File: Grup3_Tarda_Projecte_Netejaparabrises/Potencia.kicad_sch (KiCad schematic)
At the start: 47 parts, among them J8 CONNECTOR ALIMENTACIO, K1 1393280-6, K2 1393280-6, K3 1393280-6, K4 1393280-6, K5 1393280-6, K6 1393280-6, K7 1393280-6, K8 1393280-6, K9 1393280-6, Q1 BC817-25_RF, Q2 BC817-25_RF, Q3 BC817-25_RF, Q4 BC817-25_RF, Q5 BC817-25_RF, Q6 BC817-25_RF, Q7 BC817-25_RF

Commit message: Sense errors de visualització, preparat pel layout
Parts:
- J8: value CONNECTOR ALIMENTACIO -> CONNECTOR ALIMENTACIO 01x10; footprint Connector_PinHeader_2.54mm:PinHeader_1x10_P2.54mm_Vertical -> Connector_PinSocket_2.54mm:PinSocket_1x10_P2.54mm_Vertical
- K3: footprint BLM03HD331SZ1D:BEADC0603X33N -> V23076A1001C133:V23076A1001C133
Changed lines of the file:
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@@
       (effects (font (size 1.27 1.27)))
     )
-    (property "Footprint" "BLM03HD331SZ1D:BEADC0603X33N" (at 102.616 73.152 0)
+    (property "Footprint" "V23076A1001C133:V23076A1001C133" (at 102.616 73.152 0)
       (effects (font (size 1.27 1.27)) (justify bottom) hide)
     )
@@
       (effects (font (size 1.27 1.27)))
     )
-    (property "Value" "CONNECTOR ALIMENTACIO" (at 154.94 106.934 0)
-      (effects (font (size 1.27 1.27)))
-    )
-    (property "Footprint" "Connector_PinHeader_2.54mm:PinHeader_1x10_P2.54mm_Vertical" (at 143.764 122.682 0)
-      (effects (font (size 1.27 1.27)) hide)
-    )
+    (property "Value" "CONNECTOR ALIMENTACIO 01x10" (at 154.94 106.934 0)
+      (effects (font (size 1.27 1.27)))
+    )
+    (property "Footprint" "Connector_PinSocket_2.54mm:PinSocket_1x10_P2.54mm_Vertical" (at 143.764 122.682 0)
+      (effects (font (size 1.27 1.27)) hide)
+    )

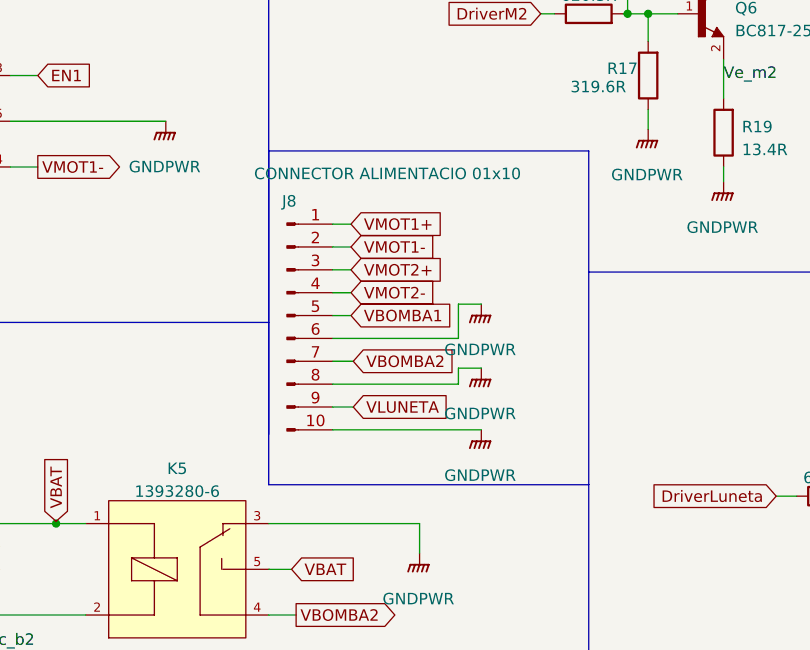
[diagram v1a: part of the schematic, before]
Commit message: canvis divisor sensor de pluja, node vbat protegit, connector de motors, README
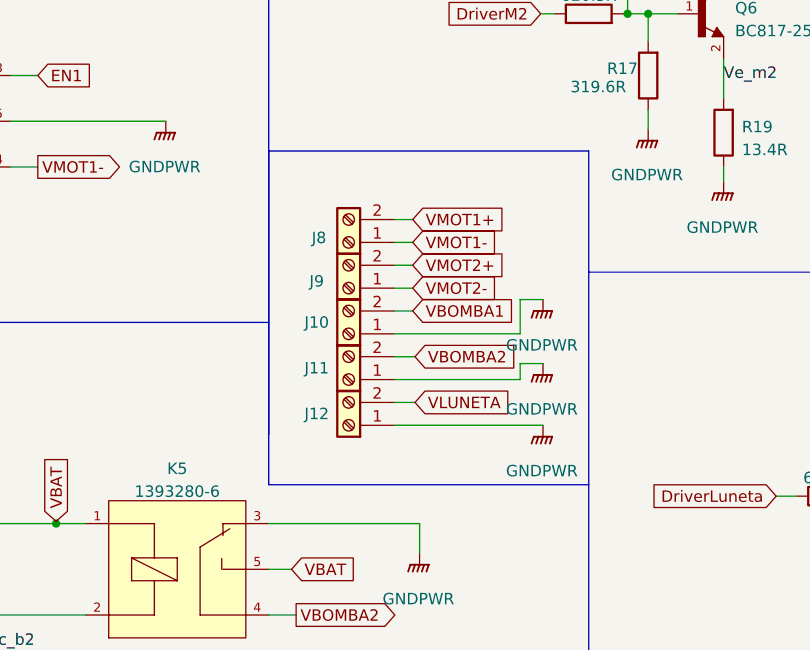
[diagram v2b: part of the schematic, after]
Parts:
- removed J8: CONNECTOR ALIMENTACIO 01x10, Connector_PinSocket_2.54mm:PinSocket_1x10_P2.54mm_Vertical, symbol Connector:Conn_01x10_Pin
- added J10, J11, J12, J8, J9: Screw_Terminal_01x02, TerminalBlock_Phoenix:TerminalBlock_Phoenix_MKDS-1,5-2-5.08_1x02_P5.08mm_Horizontal, symbol Connector:Screw_Terminal_01x02
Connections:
- net GNDPWR: now also J10.1 (Pin_1), J11.1 (Pin_1), J12.1 (Pin_1)
- net VBOMBA1: now also J10.2 (Pin_2)
- net VBOMBA2: now also J11.2 (Pin_2)
- net VLUNETA: now also J12.2 (Pin_2)
- net VMOT1+: now also J8.2 (Pin_2)
- net VMOT1-: now also J8.1 (Pin_1)
- net VMOT2+: now also J9.2 (Pin_2)
- net VMOT2-: now also J9.1 (Pin_1)

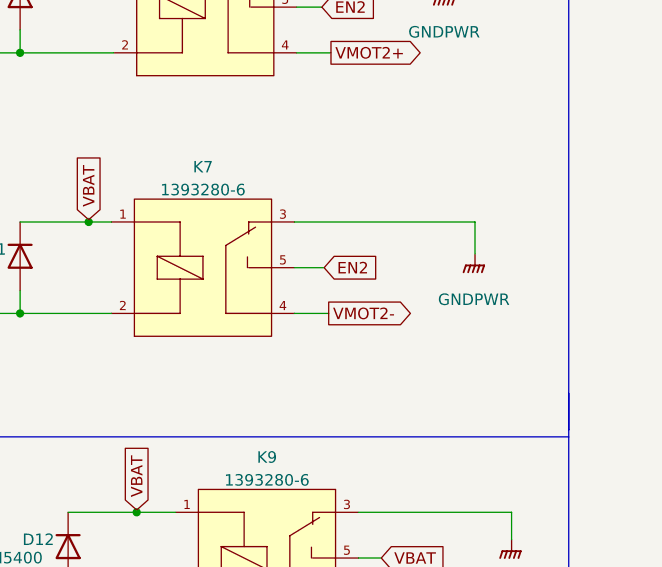
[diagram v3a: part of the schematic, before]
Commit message: placing rooting
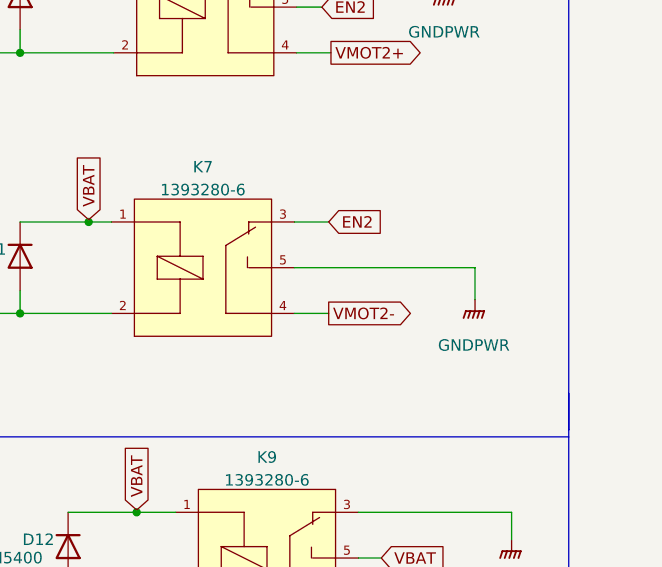
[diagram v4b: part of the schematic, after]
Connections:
- net EN2: now also K7.3; no longer K7.5
- net GNDPWR: now also K7.5; no longer K7.3
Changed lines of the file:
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@@
+    (stroke (width 0) (type default))
+  )
+  (wire (pts (xy 249.682 93.98) (xy 253.492 93.98))
     (stroke (width 0) (type default))
   )
@@
     (stroke (width 0) (type default))
   )
-  (wire (pts (xy 269.748 93.98) (xy 249.682 93.98))
-    (stroke (width 0) (type default))
-  )
   (wire (pts (xy 208.28 75.184) (xy 208.28 104.14))
     (stroke (width 0) (type default))
@@
     (stroke (width 0) (type default))
   )
-  (wire (pts (xy 249.682 99.06) (xy 252.984 99.06))
+  (wire (pts (xy 249.682 99.06) (xy 269.748 99.06))
     (stroke (width 0) (type default))
   )
@@
     (stroke (width 0) (type default))
   )
+  (wire (pts (xy 269.748 99.06) (xy 269.748 102.616))
+    (stroke (width 0) (type default))
+  )
   (wire (pts (xy 181.61 85.852) (xy 181.61 89.154))
     (stroke (width 0) (type default))
@@
   )
   (wire (pts (xy 90.17 167.894) (xy 91.694 167.894))
-    (stroke (width 0) (type default))
-  )
-  (wire (pts (xy 269.748 93.98) (xy 269.748 97.536))
     (stroke (width 0) (type default))
   )
@@
     )
   )
-  (global_label "EN2" (shape input) (at 252.984 99.06 0) (fields_autoplaced)
-    (effects (font (size 1.27 1.27)) (justify left))
-    (property "Intersheetrefs" "${INTERSHEET_REFS}" (at 259.5788 99.06 0)
+  (global_label "EN2" (shape input) (at 253.492 93.98 0) (fields_autoplaced)
+    (effects (font (size 1.27 1.27)) (justify left))
+    (property "Intersheetrefs" "${INTERSHEET_REFS}" (at 260.0868 93.98 0)
       (effects (font (size 1.27 1.27)) (justify left) hide)
     )
@@
     )
   )
-  (symbol (lib_id "power:GNDPWR") (at 269.748 97.536 0) (unit 1)
-    (in_bom yes) (on_board yes) (dnp no) (fields_autoplaced)
-    (property "Reference" "#PWR025" (at 269.748 102.616 0)
-      (effects (font (size 1.27 1.27)) hide)
-    )
-    (property "Value" "GNDPWR" (at 269.621 102.616 0)
-      (effects (font (size 1.27 1.27)))
-    )
-    (property "Footprint" "" (at 269.748 98.806 0)
-      (effects (font (size 1.27 1.27)) hide)
-    )
-    (property "Datasheet" "" (at 269.748 98.806 0)
-      (effects (font (size 1.27 1.27)) hide)
-    )
+  (symbol (lib_id "power:GNDPWR") (at 269.748 102.616 0) (unit 1)
+    (in_bom yes) (on_board yes) (dnp no) (fields_autoplaced)
+    (property "Reference" "#PWR025" (at 269.748 107.696 0)
+      (effects (font (size 1.27 1.27)) hide)
+    )
+    (property "Value" "GNDPWR" (at 269.621 107.696 0)
+      (effects (font (size 1.27 1.27)))
+    )
+    (property "Footprint" "" (at 269.748 103.886 0)
+      (effects (font (size 1.27 1.27)) hide)
+    )
+    (property "Datasheet" "" (at 269.748 103.886 0)
+      (effects (font (size 1.27 1.27)) hide)
+    )
